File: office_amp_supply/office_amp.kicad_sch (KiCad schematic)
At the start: 50 parts, among them J1 Jack-DC, J2 Conn_01x09_Socket, Q1 DMT6012LSS, U1 LM74700, U13 LM2576HVT-ADJ, U2 LM7805_TO220, U4 TBA_2-2421, U7 VXO78012_TO220

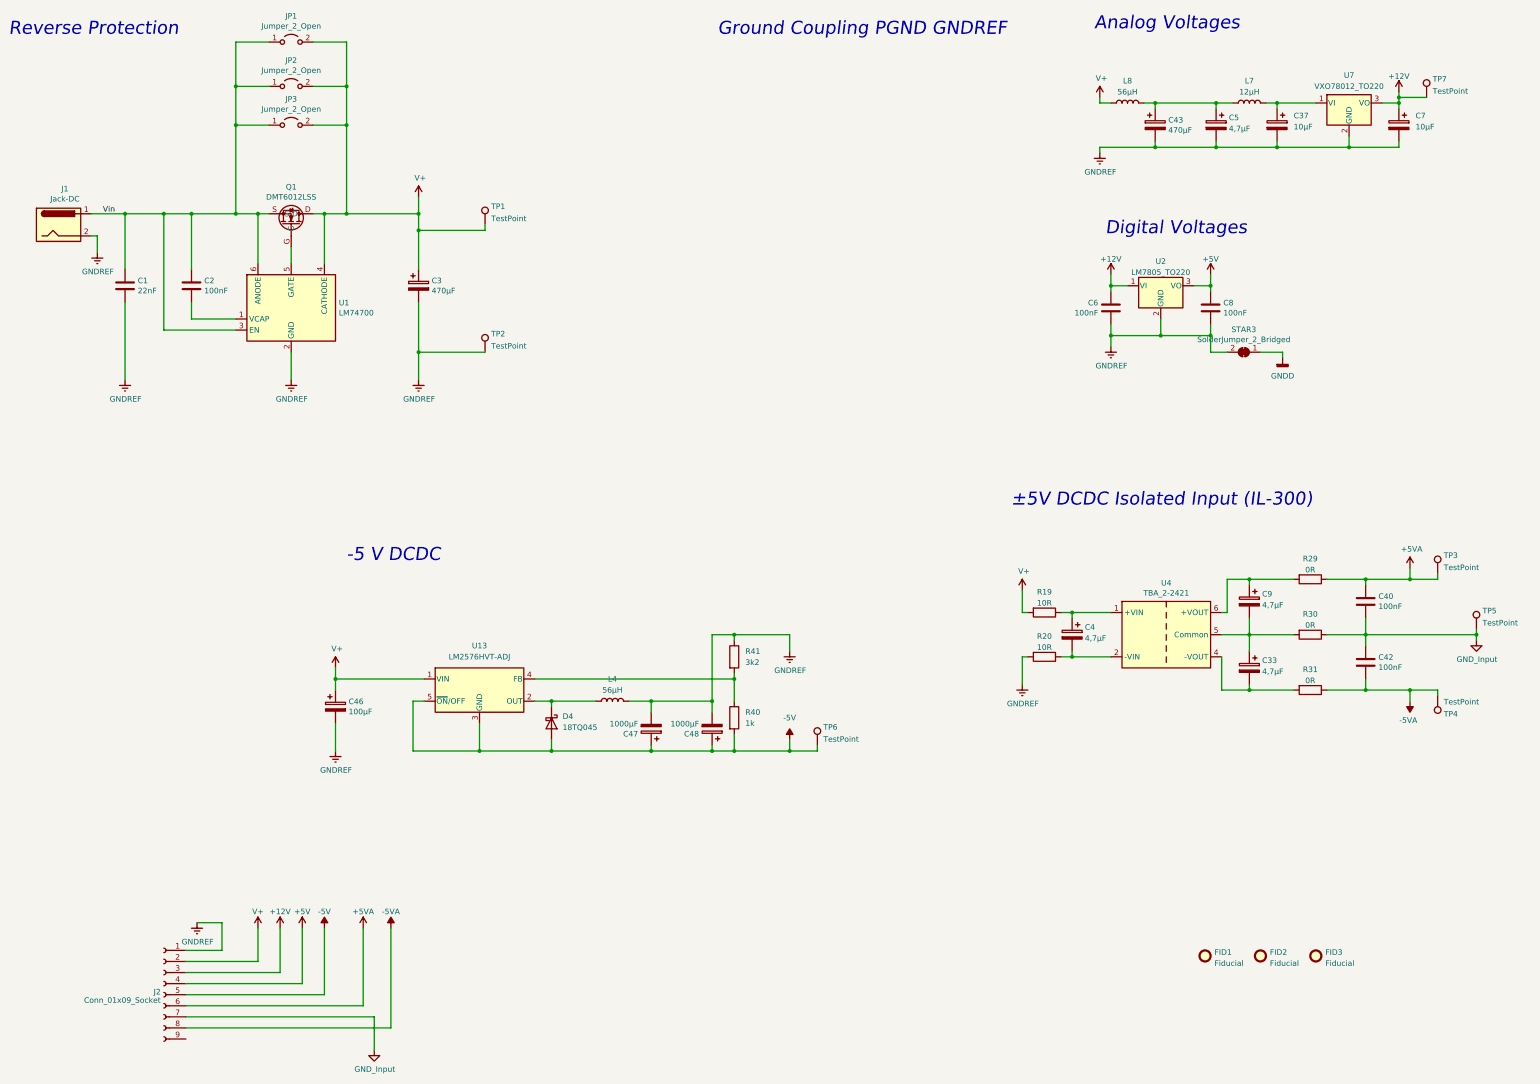
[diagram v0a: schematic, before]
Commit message: first positioning office-amp
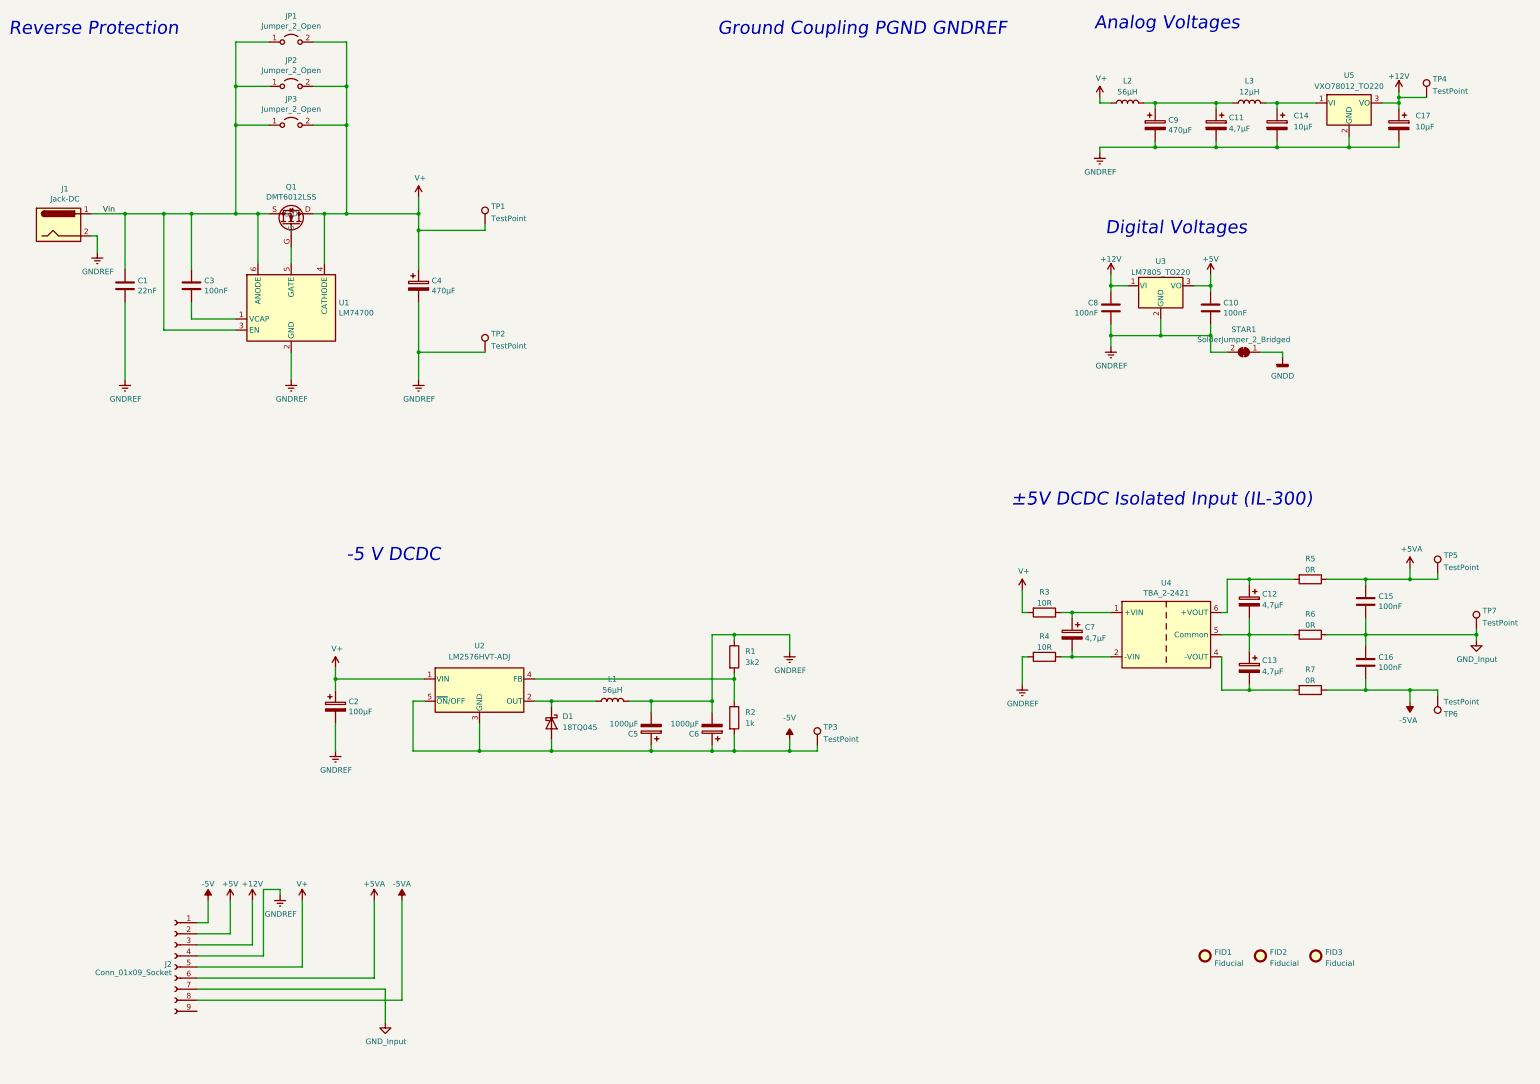
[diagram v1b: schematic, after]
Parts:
- J2: footprint Connector_Dsub:DSUB-9_Female_Horizontal_P2.77x2.84mm_EdgePinOffset4.94mm_Housed_MountingHolesOffset7.48mm -> Connector_Dsub:DSUB-9_Male_Horizontal_P2.77x2.84mm_EdgePinOffset4.94mm_Housed_MountingHolesOffset7.48mm
- renumbered C8 to C10, C5 to C11, C9 to C12, C33 to C13, C37 to C14, C40 to C15, C42 to C16, C7 to C17, C46 to C2, C2 to C3, C3 to C4, C47 to C5, C48 to C6, C4 to C7, C6 to C8, C43 to C9, D4 to D1, L4 to L1, L8 to L2, L7 to L3, R41 to R1, R40 to R2, R19 to R3, R20 to R4, R29 to R5, R30 to R6, R31 to R7, STAR3 to STAR1, TP6 to TP3, TP7 to TP4, TP3 to TP5, TP4 to TP6, TP5 to TP7, U13 to U2, U2 to U3, U7 to U5
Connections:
- net +5V: now also J2.2 (Pin_2); no longer J2.4 (Pin_4)
- net -5V: now also J2.1 (Pin_1); no longer J2.5 (Pin_5)
- net GNDREF: now also J2.4 (Pin_4); no longer J2.1 (Pin_1)
- net V+: now also J2.5 (Pin_5); no longer J2.2 (Pin_2)

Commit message: first prototype supply
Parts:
- removed STAR1: SolderJumper_2_Bridged, Jumper:SolderJumper-2_P1.3mm_Bridged_RoundedPad1.0x1.5mm, symbol Jumper:SolderJumper_2_Bridged
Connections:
- net -5V: now also C5.2, C6.2; no longer C5.1, C6.1
- net GNDD: now also C1.2, C10.2, C11.2, C14.2, C17.2, C2.2, C4.2, C5.1, C6.1, C8.2, C9.2, J1.2, J2.4 (Pin_4), J2.9 (Pin_9), L1.2, R1.1, R4.2, TP2.1, U1.2 (GND), U3.2 (GND), U5.2 (GND)
- removed net GNDREF: C1.2, C10.2, C11.2, C14.2, C17.2, C2.2, C4.2, C5.2, C6.2, C8.2, C9.2, J1.2, J2.4 (Pin_4), L1.2, R1.1, R4.2, TP2.1, U1.2 (GND), U3.2 (GND), U5.2 (GND)
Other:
- moved on the sheet: C5, C6
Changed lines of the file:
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@@
+    (stroke (width 0) (type default))
+  )
+  (wire (pts (xy 74.93 257.81) (xy 74.93 259.08))
     (stroke (width 0) (type default))
   )
@@
     (stroke (width 0) (type default))
   )
+  (wire (pts (xy 72.39 257.81) (xy 74.93 257.81))
+    (stroke (width 0) (type default))
+  )
   (wire (pts (xy 279.4 59.69) (xy 279.4 60.96))
     (stroke (width 0) (type default))
@@
     (stroke (width 0) (type default))
   )
-  (wire (pts (xy 316.23 106.68) (xy 321.31 106.68))
-    (stroke (width 0) (type default))
-  )
   (wire (pts (xy 124.46 186.69) (xy 121.92 186.69))
     (stroke (width 0) (type default))
@@
     (stroke (width 0) (type default))
   )
-  (wire (pts (xy 308.61 106.68) (xy 304.8 106.68))
+  (wire (pts (xy 304.8 106.68) (xy 321.31 106.68))
     (stroke (width 0) (type default))
   )
@@
     )
   )
-  (symbol (lib_id "Device:CP") (at 176.53 193.04 180) (unit 1)
-    (in_bom yes) (on_board yes) (dnp no)
-    (property "Reference" "C5" (at 173.5328 194.2084 0)
-      (effects (font (size 1.27 1.27)) (justify left))
-    )
-    (property "Value" "1000µF" (at 173.5328 191.897 0)
-      (effects (font (size 1.27 1.27)) (justify left))
-    )
-    (property "Footprint" "Capacitor_THT:CP_Radial_D13.0mm_P5.00mm" (at 175.5648 189.23 0)
+  (symbol (lib_id "Device:CP") (at 176.53 193.04 0) (unit 1)
+    (in_bom yes) (on_board yes) (dnp no)
+    (property "Reference" "C5" (at 179.5272 191.8716 0)
+      (effects (font (size 1.27 1.27)) (justify left))
+    )
+    (property "Value" "1000µF" (at 179.5272 194.183 0)
+      (effects (font (size 1.27 1.27)) (justify left))
+    )
+    (property "Footprint" "Capacitor_THT:CP_Radial_D13.0mm_P5.00mm" (at 177.4952 196.85 0)
       (effects (font (size 1.27 1.27)) hide)
     )
@@
     )
   )
-  (symbol (lib_id "Device:CP") (at 190.5 193.04 180) (unit 1)
-    (in_bom yes) (on_board yes) (dnp no)
-    (property "Reference" "C6" (at 187.5028 194.2084 0)
-      (effects (font (size 1.27 1.27)) (justify left))
-    )
-    (property "Value" "1000µF" (at 187.5028 191.897 0)
-      (effects (font (size 1.27 1.27)) (justify left))
-    )
-    (property "Footprint" "Capacitor_THT:CP_Radial_D13.0mm_P5.00mm" (at 189.5348 189.23 0)
+  (symbol (lib_id "Device:CP") (at 190.5 193.04 0) (unit 1)
+    (in_bom yes) (on_board yes) (dnp no)
+    (property "Reference" "C6" (at 193.4972 191.8716 0)
+      (effects (font (size 1.27 1.27)) (justify left))
+    )
+    (property "Value" "1000µF" (at 193.4972 194.183 0)
+      (effects (font (size 1.27 1.27)) (justify left))
+    )
+    (property "Footprint" "Capacitor_THT:CP_Radial_D13.0mm_P5.00mm" (at 191.4652 196.85 0)
       (effects (font (size 1.27 1.27)) hide)
     )
@@
         (path "/2de1ffee-2174-41d2-8969-68b8d21e5a7d"
           (reference "#PWR03") (unit 1)
-        )
-      )
-    )
-  )
-  (symbol (lib_id "Jumper:SolderJumper_2_Bridged") (at 312.42 106.68 0) (mirror y) (unit 1)
-    (in_bom yes) (on_board yes) (dnp no)
-    (property "Reference" "STAR1" (at 312.42 101.473 0)
-      (effects (font (size 1.27 1.27)))
-    )
-    (property "Value" "SolderJumper_2_Bridged" (at 312.42 103.7844 0)
-      (effects (font (size 1.27 1.27)))
-    )
-    (property "Footprint" "Jumper:SolderJumper-2_P1.3mm_Bridged_RoundedPad1.0x1.5mm" (at 312.42 106.68 0)
-      (effects (font (size 1.27 1.27)) hide)
-    )
-    (property "Datasheet" "~" (at 312.42 106.68 0)
-      (effects (font (size 1.27 1.27)) hide)
-    )
-    (pin "1")
-    (pin "2")
-    (instances
-      (project "office_amp"
-        (path "/2de1ffee-2174-41d2-8969-68b8d21e5a7d"
-          (reference "STAR1") (unit 1)
         )
       )
@@
         )
       )
+    )
+  )
+  (symbol (lib_id "power:GNDREF") (at 74.93 259.08 0) (unit 1)
+    (in_bom yes) (on_board yes) (dnp no)
+    (property "Reference" "#PWR030" (at 74.93 265.43 0)
+      (effects (font (size 1.27 1.27)) hide)
+    )
+    (property "Value" "GNDREF" (at 75.057 263.4742 0)
+      (effects (font (size 1.27 1.27)))
+    )
+    (property "Footprint" "" (at 74.93 259.08 0)
+      (effects (font (size 1.27 1.27)) hide)
+    )
+    (property "Datasheet" "" (at 74.93 259.08 0)
+      (effects (font (size 1.27 1.27)) hide)
+    )
+    (pin "1")
+    (instances
+      (project "office_amp"
+        (path "/2de1ffee-2174-41d2-8969-68b8d21e5a7d"
+          (reference "#PWR030") (unit 1)
+        )
+      )
